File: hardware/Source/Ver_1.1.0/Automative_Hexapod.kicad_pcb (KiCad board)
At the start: 2 copper layers, 80.5 x 100 mm, 160 parts, among them J1 Pin Connector, J10 Connector, J11 Connector, J12 Connector, J13 Connector, J14 Connector, J15 Connector, J16 Connector, J17 Connector, J18 Connector, J19 Connector, J2 Connector, J20 Connector, J21 Connector, J22 Connector, J23 Connector, J24 Connector, J3 Connector, J4 MPU6050, J5 Connector, J6 Connector, J7 Connector, J8 Connector, J9 Connector, Q1 LN2302LT1G, Q2 LN2302LT1G, Q3 LN2302LT1G, SW1 MTS-102-C3, U1 TPS54331DR, U3 PCA9685PW, U4 PCA9685PW

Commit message: Generate Gerber V1.1.0
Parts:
- moved C44 0.28 mm to (111.2, 132.7)
- moved J13 0.28 mm to (112.2, 138.7)
- moved C48 0.28 mm to (111.2, 134.4)
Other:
- board size 80.5 x 100 mm -> 80.5 x 99.9 mm
- board text added: "C0_6"
- board text added: "C0_7"
- board text added: "C0_8"
- board text added: "C1_0"
- board text added: "C1_1"
- board text added: "C1_2"
- board text added: "C1_3"
- board text added: "C1_4"
- board text added: "C1_5"
- board text added: "C1_6"
- board text added: "C1_7"
- board text added: "C1_8"
- board text added: "LED 3V3"
- board text added: "LED STATUS"
- board text added: "VBAT"
- board text added: "VCC"
- board text removed: "CH1_0"
- board text removed: "CH1_1"
- board text removed: "CH1_2"
- board text removed: "CH1_3"
- board text removed: "CH1_4"
- board text removed: "CH1_5"
- board text removed: "CH1_7"
- board text removed: "CH1_8"

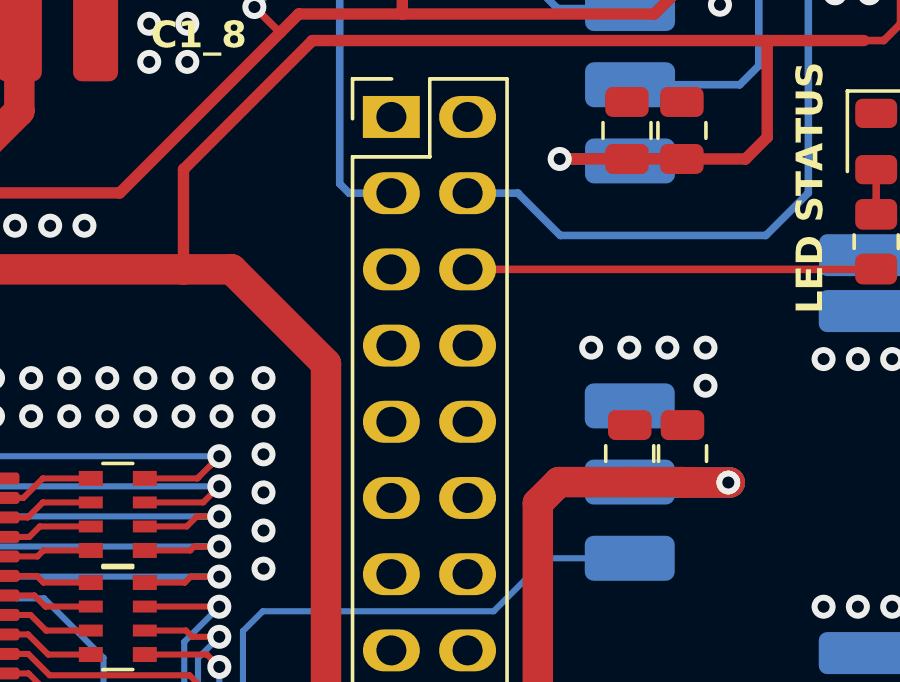
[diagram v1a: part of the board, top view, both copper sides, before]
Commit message: Generate PDF Schematic Ver1.1.0 and add README.md
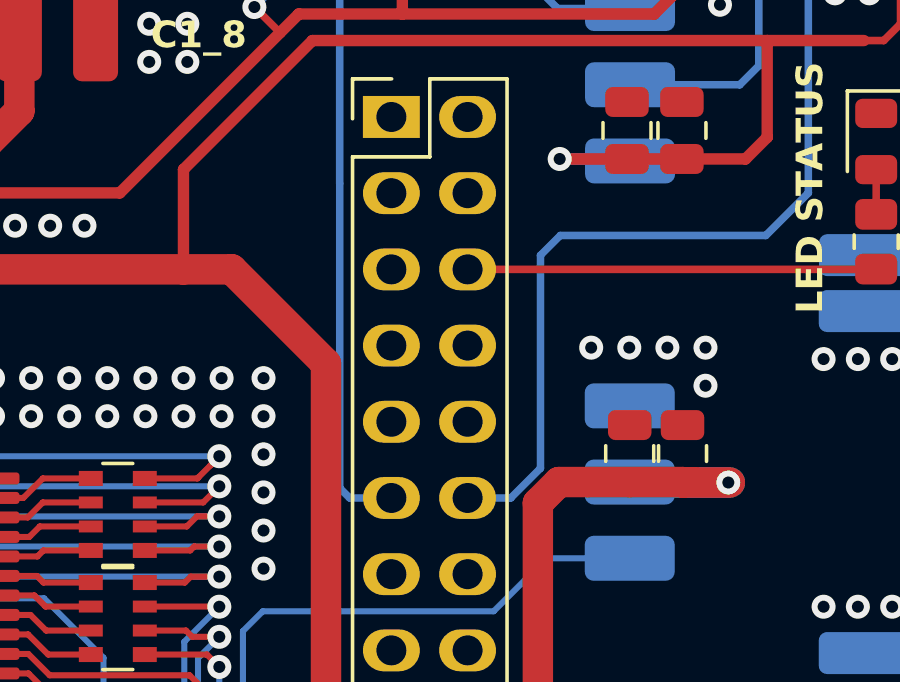
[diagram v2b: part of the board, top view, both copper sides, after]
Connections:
- net BBAI_I2C_SCL renamed BBBlack_I2C_SCL
- net BBAI_I2C_SDA renamed BBBlack_I2C_SDA
- net BBAI_PWM1A renamed BBBlack_PWM1A
- Q1 pad 2: BBAI_TRIG -> BBBlack_TRIG
- Q2 pad 2: BBAI_ECHO -> BBBlack_ECHO
- R14 pad 1: BBAI_TRIG -> BBBlack_TRIG
- R15 pad 1: BBAI_ECHO -> BBBlack_ECHO
- U2 pad P8_11: unconnected-(U2-eQEP2bB/GPIO1_13-PadP8_11) -> BBBlack_ECHO
- U2 pad P8_12: unconnected-(U2-eQEP2bA/GPIO1_12-PadP8_12) -> BBBlack_TRIG
- U2 pad P8_3: BBAI_ECHO -> unconnected-(U2-GPIO1_6-PadP8_3)
- U2 pad P8_4: BBAI_TRIG -> unconnected-(U2-GPIO1_7-PadP8_4)
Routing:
- net BBBlack_TRIG: track 0.00 -> 39.2 mm, vias 0 -> 1
- net BBAI_TRIG: track 32.0 -> 0.00 mm, vias 1 -> 0
- net BBBlack_ECHO: track 0.00 -> 29.4 mm, vias 0 -> 1
- net BBAI_ECHO: track 19.2 -> 0.00 mm, vias 1 -> 0
